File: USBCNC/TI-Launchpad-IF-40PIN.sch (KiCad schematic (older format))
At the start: 4 parts

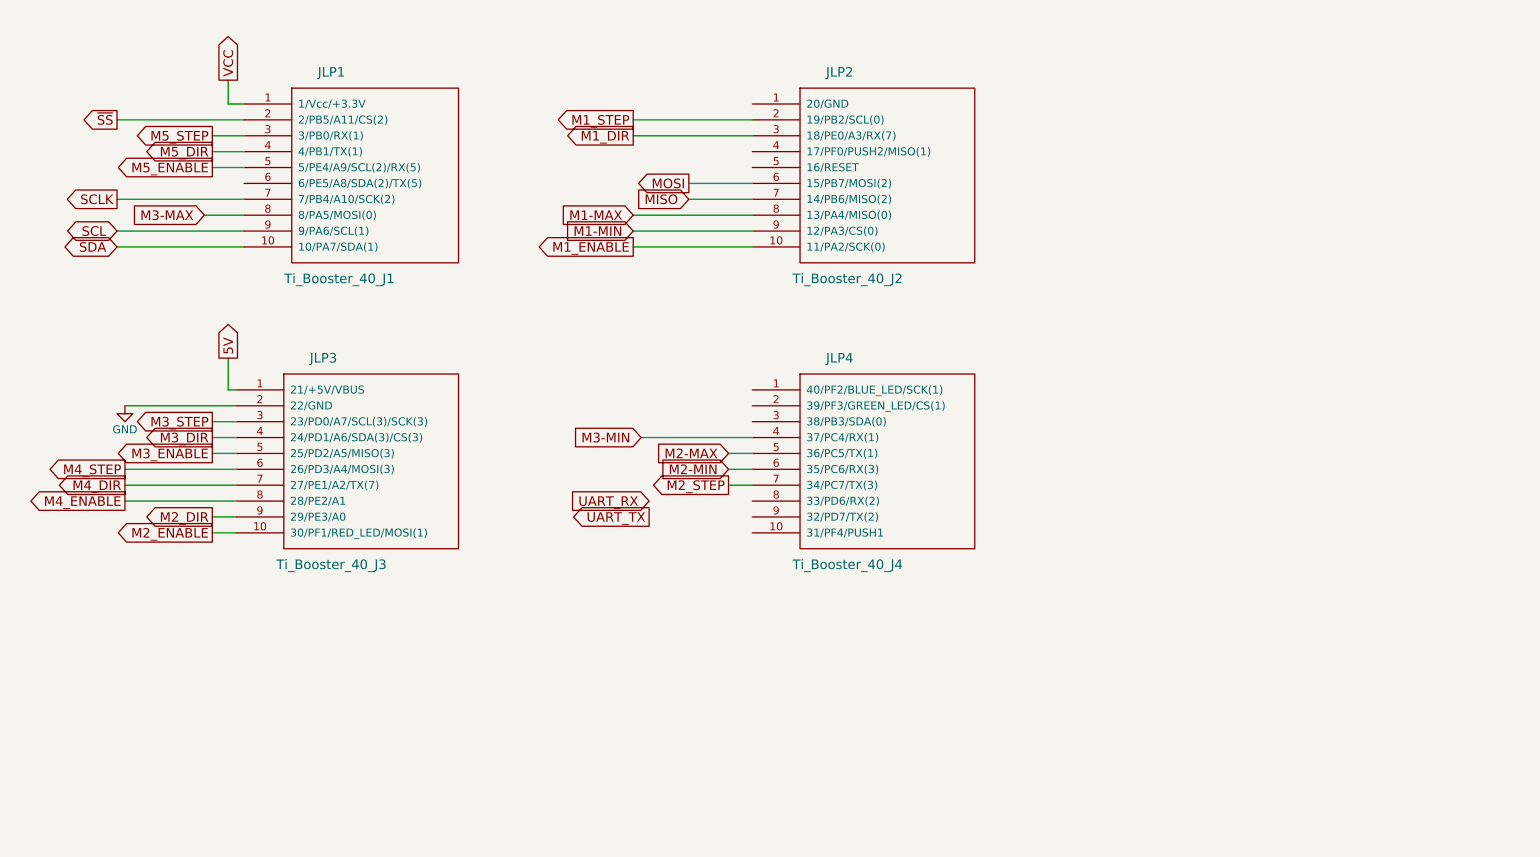
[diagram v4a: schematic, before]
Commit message: Fixing ERC
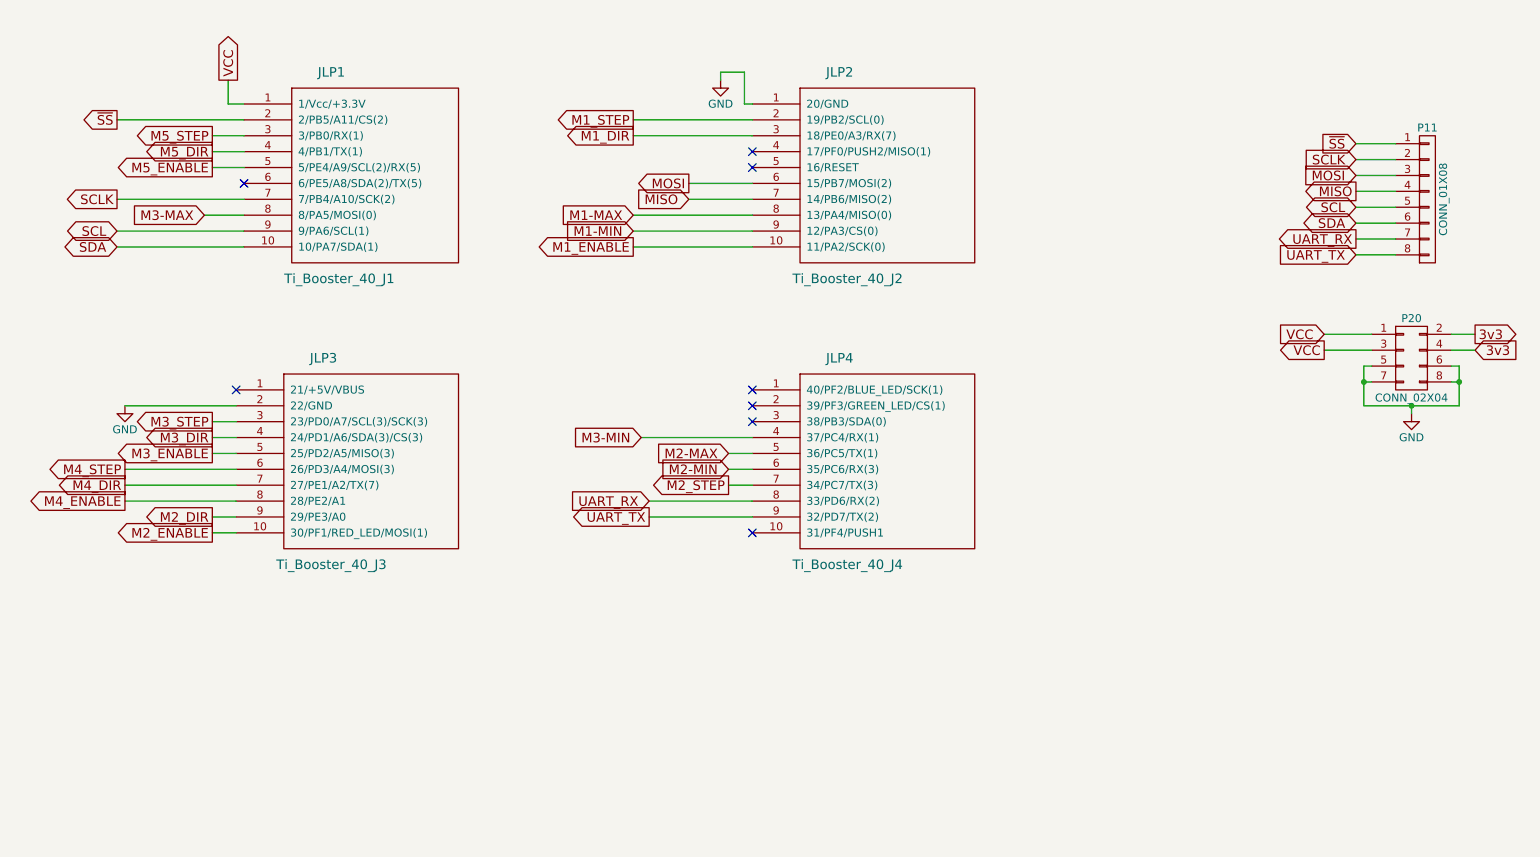
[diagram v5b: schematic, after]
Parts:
- added P11: CONN_01X08, symbol CONN_01X08
- added P20: CONN_02X04, symbol CONN_02X04
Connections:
- net GND: now also JLP2.1 (20/GND), P20.5 (P5), P20.6 (P6), P20.7 (P7), P20.8 (P8)
- net MISO: now also P11.4 (P4)
- net MOSI: now also P11.3 (P3)
- net SCL: now also P11.5 (P5)
- net SCLK: now also P11.2 (P2)
- net SDA: now also P11.6 (P6)
- net UART_RX: now also JLP4.8 (33/PD6/RX(2)), P11.7 (P7)
- net UART_TX: now also JLP4.9 (32/PD7/TX(2)), P11.8 (P8)
- net VCC: now also P20.1 (P1), P20.3 (P3)
- net ~SS: now also P11.1 (P1)
- net 5V: no longer names the net of JLP3.1 (21/+5V/VBUS)
- new net 3v3: P20.2 (P2), P20.4 (P4)
- no-connect marks 0 -> 8
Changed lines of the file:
@@
 Text GLabel 1050 2900 0    60   Output ~ 0
 SCLK
-Text GLabel 1750 3900 1    60   Output ~ 0
-5V
-$Comp
-L GND #PWR?
+$Comp
+L GND #PWR01
 U 1 1 55A2A931
 P 1100 4200
-F 0 "#PWR?" H 1100 3950 50  0001 C CNN
+F 0 "#PWR01" H 1100 3950 50  0001 C CNN
 F 1 "GND" H 1100 4050 50  0000 C CNN
 F 2 "" H 1100 4200 60  0000 C CNN
@@
 	1800 4200 1100 4200
 Wire Wire Line
-	1750 4100 1750 3900
-Wire Wire Line
 	1650 4300 1800 4300
 Wire Wire Line
@@
 Text GLabel 1050 2400 0    60   Output ~ 0
 ~SS
-Wire Wire Line
-	1850 2300 1750 2300
 Wire Wire Line
 	1750 2300 1750 2150
@@
 Wire Wire Line
 	5050 3200 4300 3200
-Wire Wire Line
-	1800 4100 1750 4100
 Text GLabel 1050 3100 0    60   BiDi ~ 0
 SCL
@@
 Text GLabel 4400 4800 0    60   Input ~ 0
 UART_RX
+NoConn ~ 1850 2800
+NoConn ~ 5050 2600
+NoConn ~ 5050 2700
+NoConn ~ 5050 4100
+NoConn ~ 5050 4200
+NoConn ~ 5050 4300
+Wire Wire Line
+	5050 4800 4400 4800
+Wire Wire Line
+	5050 4900 4400 4900
+NoConn ~ 5050 5000
+Wire Wire Line
+	1850 2300 1750 2300
+NoConn ~ 1800 4100
+$Comp
+L CONN_01X08 P11
+U 1 1 55A7FFAF
+P 9300 2900
+F 0 "P11" H 9300 3350 50  0000 C CNN
+F 1 "CONN_01X08" V 9400 2900 50  0000 C CNN
+F 2 "" H 9300 2900 60  0000 C CNN
+F 3 "" H 9300 2900 60  0000 C CNN
+	1    9300 2900
+	1    0    0    -1
+$EndComp
+$Comp
+L GND #PWR02
+U 1 1 55A8025C
+P 4850 2150
+F 0 "#PWR02" H 4850 1900 50  0001 C CNN
+F 1 "GND" H 4850 2000 50  0000 C CNN
+F 2 "" H 4850 2150 60  0000 C CNN
+F 3 "" H 4850 2150 60  0000 C CNN
+	1    4850 2150
+	-1   0    0    -1
+$EndComp
+Wire Wire Line
+	5000 2300 5000 2100
+Wire Wire Line
+	5000 2100 4850 2100
+Wire Wire Line
+	4850 2100 4850 2150
+Text GLabel 8850 2750 0    60   Input ~ 0
+MOSI
+Text GLabel 8850 2850 0    60   Output ~ 0
+MISO
+Text GLabel 8850 2650 0    60   Input ~ 0
+SCLK
+Text GLabel 8850 2550 0    60   Input ~ 0
+~SS
+Text GLabel 8850 2950 0    60   BiDi ~ 0
+SCL
+Text GLabel 8850 3050 0    60   BiDi ~ 0
+SDA
+Wire Wire Line
+	9100 2550 8850 2550
+Wire Wire Line
+	9100 2650 8850 2650
+Wire Wire Line
+	9100 2750 8850 2750
+Wire Wire Line
+	9100 3050 8850 3050
+Wire Wire Line
+	9100 2850 8850 2850
+Wire Wire Line
+	9100 2950 8850 2950
+Wire Wire Line
+	5050 2300 5000 2300
+Text GLabel 8850 3250 0    60   Input ~ 0
+UART_TX
+Text GLabel 8850 3150 0    60   Output ~ 0
+UART_RX
+Wire Wire Line
+	9100 3150 8850 3150
+Wire Wire Line
+	9100 3250 8850 3250
+$Comp
+L CONN_02X04 P20
+U 1 1 55A81992
+P 9200 3900
+F 0 "P20" H 9200 4150 50  0000 C CNN
+F 1 "CONN_02X04" H 9200 3650 50  0000 C CNN
+F 2 "" H 9200 2700 60  0000 C CNN
+F 3 "" H 9200 2700 60  0000 C CNN
+	1    9200 3900
+	1    0    0    -1
+$EndComp
+Text GLabel 9600 3750 2    60   Output ~ 0
+3v3
+Wire Wire Line
+	9450 3750 9600 3750
+Text GLabel 8650 3750 0    60   Input ~ 0
+VCC
+Wire Wire Line
+	8950 3750 8650 3750
+Wire Wire Line
+	8950 4050 8900 4050
+Wire Wire Line
+	8900 3950 8900 4200
+Wire Wire Line
+	8900 4200 9500 4200
+Wire Wire Line
+	9500 4200 9500 3950
+Wire Wire Line
+	9500 4050 9450 4050
+$Comp
+L GND #PWR03
+U 1 1 55A81E90
+P 9200 4250
+F 0 "#PWR03" H 9200 4000 50  0001 C CNN
+F 1 "GND" H 9200 4100 50  0000 C CNN
+F 2 "" H 9200 4250 60  0000 C CNN
+F 3 "" H 9200 4250 60  0000 C CNN
+	1    9200 4250
+	-1   0    0    -1
+$EndComp
+Wire Wire Line
+	9200 4250 9200 4200
+Connection ~ 9200 4200
+Text GLabel 9600 3850 2    60   Input ~ 0
+3v3
+Wire Wire Line
+	9600 3850 9450 3850
+Wire Wire Line
+	8650 3850 8950 3850
+Wire Wire Line
+	9500 3950 9450 3950
+Connection ~ 9500 4050
+Wire Wire Line
+	8950 3950 8900 3950
+Connection ~ 8900 4050
+Text GLabel 8650 3850 0    60   Output ~ 0
+VCC
 $EndSCHEMATC
